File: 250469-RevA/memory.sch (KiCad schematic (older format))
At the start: 10 parts, among them U10 41464, U11 41464, U19 2114, U22 7416, U3 74LS08, U8 251715-01

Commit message: Change footprint of PLA to Socket version
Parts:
- U8: footprint krl_Package_SPDIP:SPDIP-64_W19.05mm_LongPads -> krl_Package_SPDIP:SPDIP-64_W19.05mm_Socket_LongPads
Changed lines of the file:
@@
 F 0 "U8" H 8000 5700 50  0000 C CNN
 F 1 "251715-01" H 8900 5700 50  0000 C CNN
-F 2 "krl_Package_SPDIP:SPDIP-64_W19.05mm_LongPads" H 7600 2100 50  0001 C CNN
+F 2 "krl_Package_SPDIP:SPDIP-64_W19.05mm_Socket_LongPads" H 7600 2100 50  0001 C CNN
 F 3 "" H 8600 5050 50  0001 C CNN
 	1    8550 3950

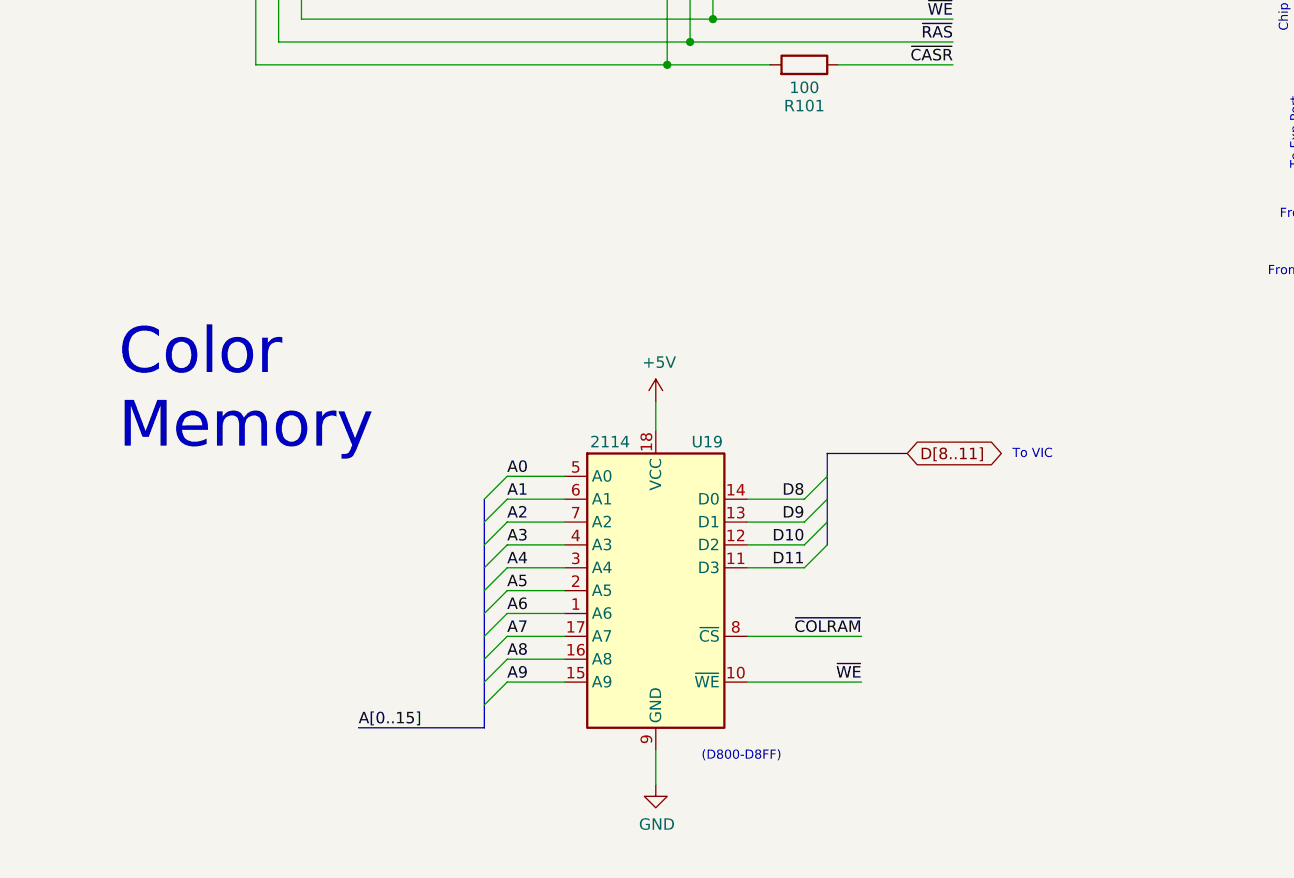
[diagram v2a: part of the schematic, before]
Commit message: Changed footprint of DIC connectors and wiring of Color RAM
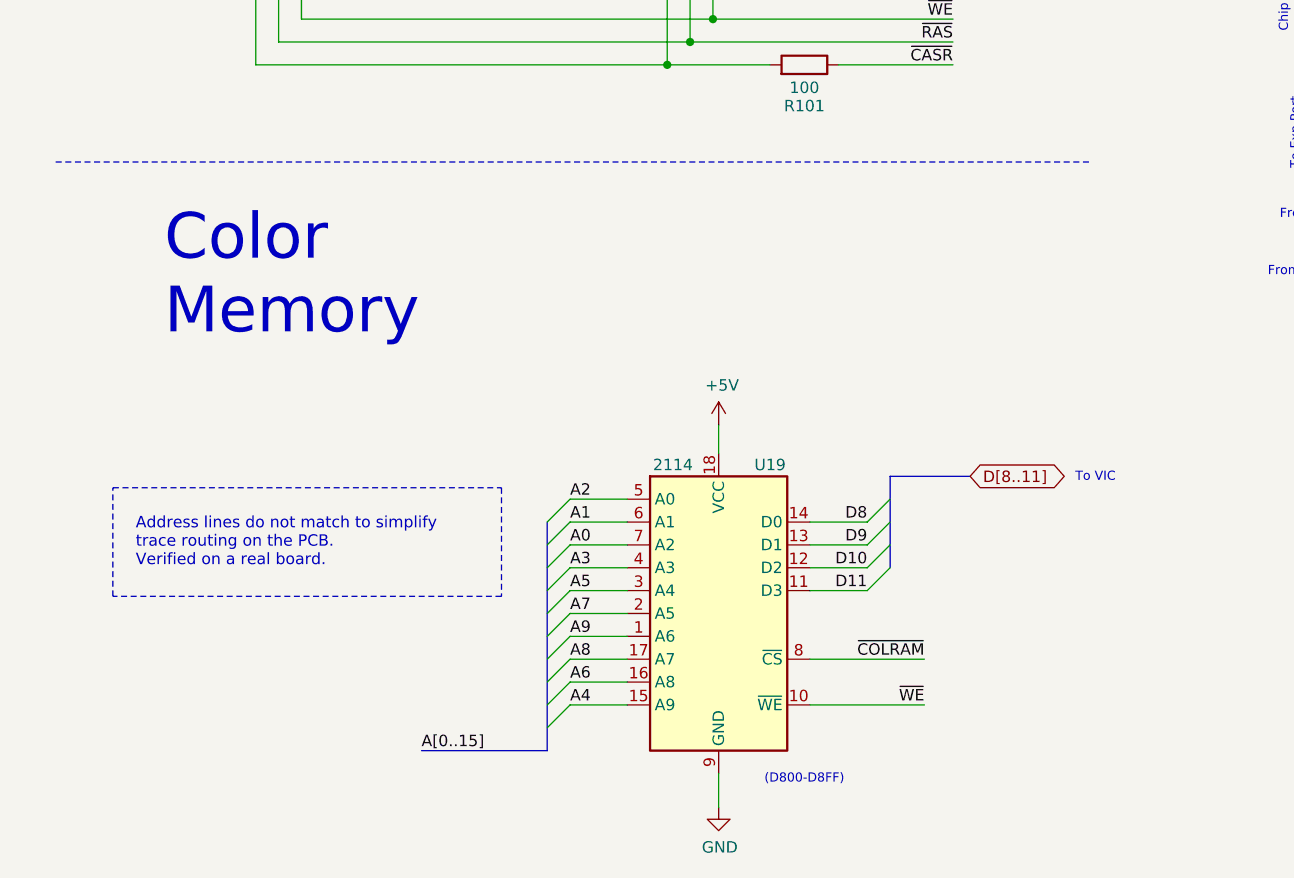
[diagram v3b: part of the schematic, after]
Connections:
- net A0: now also U19.7 (A2); no longer U19.5 (A0)
- net A2: now also U19.5 (A0); no longer U19.7 (A2)
- net A4: now also U19.15 (A9); no longer U19.3 (A4)
- net A5: now also U19.3 (A4); no longer U19.2 (A5)
- net A6: now also U19.16 (A8); no longer U19.1 (A6)
- net A7: now also U19.2 (A5); no longer U19.17 (A7)
- net A8: now also U19.17 (A7); no longer U19.16 (A8)
- net A9: now also U19.1 (A6); no longer U19.15 (A9)
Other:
- note added: "Address lines do not match to simplify\ntrace routing on the PCB.\nVerified on a real board."
- moved on the sheet: U19
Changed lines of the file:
@@
 Text Label 7400 3950 0    50   ~ 0
 ~WE
-Text Label 2200 6650 0    50   ~ 0
+Text Label 2475 6750 0    50   ~ 0
 A[0..15]
 Wire Wire Line
@@
  Memory\nController
 Wire Wire Line
-	3100 5550 2850 5550
-Entry Wire Line
-	2850 5550 2750 5650
-Entry Wire Line
-	2850 5650 2750 5750
-Entry Wire Line
-	2850 5750 2750 5850
-Entry Wire Line
-	2850 5850 2750 5950
-Entry Wire Line
-	2850 5950 2750 6050
-Entry Wire Line
-	2850 6050 2750 6150
-Entry Wire Line
-	2850 6150 2750 6250
-Entry Wire Line
-	2850 6250 2750 6350
-Entry Wire Line
-	2850 6350 2750 6450
-Entry Wire Line
-	2850 6450 2750 6550
-Wire Wire Line
-	2850 6450 3100 6450
-Wire Wire Line
-	2850 6350 3100 6350
-Wire Wire Line
-	2850 6250 3100 6250
-Wire Wire Line
-	2850 6150 3100 6150
-Wire Wire Line
-	2850 6050 3100 6050
-Wire Wire Line
-	2850 5950 3100 5950
-Wire Wire Line
-	2850 5850 3100 5850
-Wire Wire Line
-	2850 5650 3100 5650
-Wire Wire Line
-	2850 5750 3100 5750
-Text Label 2850 5550 0    50   ~ 0
+	3375 5650 3125 5650
+Entry Wire Line
+	3125 5650 3025 5750
+Entry Wire Line
+	3125 5750 3025 5850
+Entry Wire Line
+	3125 5850 3025 5950
+Entry Wire Line
+	3125 5950 3025 6050
+Entry Wire Line
+	3125 6050 3025 6150
+Entry Wire Line
+	3125 6150 3025 6250
+Entry Wire Line
+	3125 6250 3025 6350
+Entry Wire Line
+	3125 6350 3025 6450
+Entry Wire Line
+	3125 6450 3025 6550
+Entry Wire Line
+	3125 6550 3025 6650
+Wire Wire Line
+	3125 6550 3375 6550
+Wire Wire Line
+	3125 6450 3375 6450
+Wire Wire Line
+	3125 6350 3375 6350
+Wire Wire Line
+	3125 6250 3375 6250
+Wire Wire Line
+	3125 6150 3375 6150
+Wire Wire Line
+	3125 6050 3375 6050
+Wire Wire Line
+	3125 5950 3375 5950
+Wire Wire Line
+	3125 5750 3375 5750
+Wire Wire Line
+	3125 5850 3375 5850
+Text Label 3125 5850 0    50   ~ 0
 A0
-Text Label 2850 5650 0    50   ~ 0
+Text Label 3125 5750 0    50   ~ 0
 A1
-Text Label 2850 5750 0    50   ~ 0
+Text Label 3125 5650 0    50   ~ 0
 A2
-Text Label 2850 5850 0    50   ~ 0
+Text Label 3125 5950 0    50   ~ 0
 A3
-Text Label 2850 5950 0    50   ~ 0
+Text Label 3125 6550 0    50   ~ 0
 A4
-Text Label 2850 6050 0    50   ~ 0
+Text Label 3125 6050 0    50   ~ 0
 A5
-Text Label 2850 6150 0    50   ~ 0
+Text Label 3125 6450 0    50   ~ 0
 A6
-Text Label 2850 6250 0    50   ~ 0
+Text Label 3125 6150 0    50   ~ 0
 A7
-Text Label 2850 6350 0    50   ~ 0
+Text Label 3125 6350 0    50   ~ 0
 A8
-Text Label 2850 6450 0    50   ~ 0
+Text Label 3125 6250 0    50   ~ 0
 A9
 $Comp
 L power:GND #PWR0173
 U 1 1 5F0F4C6A
-P 3500 6900
-F 0 "#PWR0173" H 3500 6650 50  0001 C CNN
-F 1 "GND" H 3505 6727 50  0000 C CNN
-F 2 "" H 3500 6900 50  0001 C CNN
-F 3 "" H 3500 6900 50  0001 C CNN
-	1    3500 6900
+P 3775 7000
+F 0 "#PWR0173" H 3775 6750 50  0001 C CNN
+F 1 "GND" H 3780 6827 50  0000 C CNN
+F 2 "" H 3775 7000 50  0001 C CNN
+F 3 "" H 3775 7000 50  0001 C CNN
+	1    3775 7000
 	1    0    0    -1
 $EndComp
 Wire Wire Line
-	3900 6250 4400 6250
-Wire Wire Line
-	3900 6450 4400 6450
-Wire Wire Line
-	3900 5950 4150 5950
-Wire Wire Line
-	3900 5650 4150 5650
-Wire Wire Line
-	3900 5750 4150 5750
-Wire Wire Line
-	3900 5850 4150 5850
-Entry Wire Line
-	4150 5650 4250 5550
-Entry Wire Line
-	4150 5750 4250 5650
-Entry Wire Line
-	4150 5850 4250 5750
-Entry Wire Line
-	4150 5950 4250 5850
-Wire Bus Line
-	4250 5450 4600 5450
-Text GLabel 4600 5450 2    50   BiDi ~ 0
+	4175 6350 4675 6350
+Wire Wire Line
+	4175 6550 4675 6550
+Wire Wire Line
+	4175 6050 4425 6050
+Wire Wire Line
+	4175 5750 4425 5750
+Wire Wire Line
+	4175 5850 4425 5850
+Wire Wire Line
+	4175 5950 4425 5950
+Entry Wire Line
+	4425 5750 4525 5650
+Entry Wire Line
+	4425 5850 4525 5750
+Entry Wire Line
+	4425 5950 4525 5850
+Entry Wire Line
+	4425 6050 4525 5950
+Wire Bus Line
+	4525 5550 4875 5550
+Text GLabel 4875 5550 2    50   BiDi ~ 0
 D[8..11]
-Text Label 4150 5650 2    50   ~ 0
+Text Label 4425 5750 2    50   ~ 0
 D8
-Text Label 4150 5750 2    50   ~ 0
+Text Label 4425 5850 2    50   ~ 0
 D9
-Text Label 4150 5850 2    50   ~ 0
+Text Label 4425 5950 2    50   ~ 0
 D10
-Text Label 4150 5950 2    50   ~ 0
+Text Label 4425 6050 2    50   ~ 0
 D11
 Wire Wire Line
@@
 Text Label 7400 4050 0    50   ~ 0
 ~COLRAM
-Text Label 4400 6250 2    50   ~ 0
+Text Label 4675 6350 2    50   ~ 0
 ~COLRAM
 Text Notes 3000 950  0    200  ~ 0
 RAM
-Text Notes 1150 5450 0    200  ~ 0
+Text Notes 1350 4950 0    200  ~ 0
 Color\nMemory
-Text Label 4400 6450 2    50   ~ 0
+Text Label 4675 6550 2    50   ~ 0
 ~WE
-Text Notes 3700 6800 0    40   ~ 0
+Text Notes 3975 6900 0    40   ~ 0
 (D800-D8FF)
 Text GLabel 7050 5500 0    50   BiDi ~ 0
@@
 	7700 5550 7950 5550
 Wire Bus Line
-	2750 6650 2200 6650
+	3025 6750 2475 6750
 Text GLabel 10300 2150 2    50   Output ~ 0
 ~KBR_CS
@@
 Text Notes 6480 4680 2    40   ~ 0
 From CIA 2
-Text Notes 5060 5480 0    40   ~ 0
+Text Notes 5335 5580 0    40   ~ 0
 To VIC
 Wire Wire Line
@@
 L power:+5V #PWR0172
 U 1 1 5EFDEDE2
-P 3500 5225
-F 0 "#PWR0172" H 3500 5075 50  0001 C CNN
-F 1 "+5V" H 3515 5398 50  0000 C CNN
-F 2 "" H 3500 5225 50  0001 C CNN
-F 3 "" H 3500 5225 50  0001 C CNN
-	1    3500 5225
+P 3775 5325
+F 0 "#PWR0172" H 3775 5175 50  0001 C CNN
+F 1 "+5V" H 3790 5498 50  0000 C CNN
+F 2 "" H 3775 5325 50  0001 C CNN
+F 3 "" H 3775 5325 50  0001 C CNN
+	1    3775 5325
 	1    0    0    -1
 $EndComp
@@
 L krl_Memory_RAM:2114 U19
 U 1 1 5E3F3F3A
-P 3500 6050
-F 0 "U19" H 3725 6700 50  0000 C CNN
-F 1 "2114" H 3300 6700 50  0000 C CNN
-F 2 "Package_DIP:DIP-18_W7.62mm_Socket" H 2750 5400 50  0001 C CIN
-F 3 "" H 3500 6150 50  0001 C CNN
-	1    3500 6050
+P 3775 6150
+F 0 "U19" H 4000 6800 50  0000 C CNN
+F 1 "2114" H 3575 6800 50  0000 C CNN
+F 2 "Package_DIP:DIP-18_W7.62mm_Socket" H 3025 5500 50  0001 C CIN
+F 3 "" H 3775 6250 50  0001 C CNN
+	1    3775 6150
 	1    0    0    -1
 $EndComp
 Wire Wire Line
-	3500 5225 3500 5350
-Wire Wire Line
-	3500 6900 3500 6750
+	3775 5325 3775 5450
+Wire Wire Line
+	3775 7000 3775 6850
 Wire Wire Line
 	2500 3200 2500 2925
@@
 Wire Wire Line
 	4300 2925 4300 3000
+Wire Notes Line
+	875  4175 5400 4175
+Text Notes 1225 5950 0    50   ~ 0
+Address lines do not match to simplify\ntrace routing on the PCB.\nVerified on a real board.
+Wire Notes Line width 10 style solid
+	1125 5600 2825 5600
+Wire Notes Line width 10 style solid
+	2825 5600 2825 6075
+Wire Notes Line width 10 style solid
+	2825 6075 1125 6075
+Wire Notes Line width 10 style solid
+	1125 6075 1125 5600
 Wire Bus Line
 	7250 4450 7250 4650
@@
 	7150 4250 7150 4400
 Wire Bus Line
-	4250 5450 4250 5850
+	4525 5550 4525 5950
 Wire Bus Line
 	1650 1950 1650 3050
@@
 	7500 4750 7500 5500
 Wire Bus Line
-	2750 5650 2750 6650
+	3025 5750 3025 6750
 Wire Bus Line
 	5050 1500 5050 2450

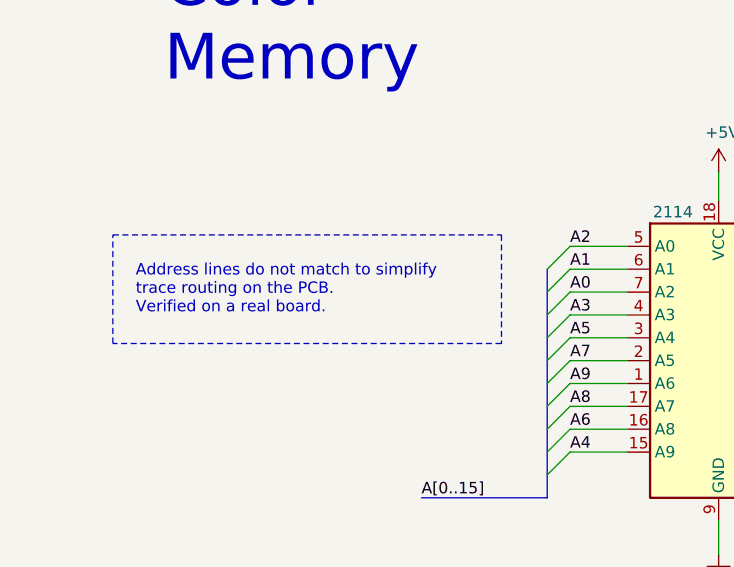
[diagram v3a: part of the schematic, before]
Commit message: Minor changes to the memory sheet
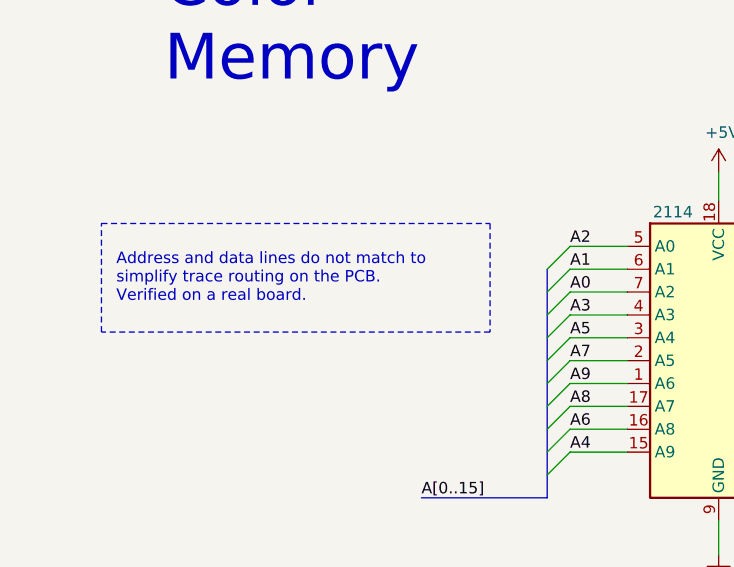
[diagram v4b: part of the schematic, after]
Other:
- note added: "Address and data lines do not match to\nsimplify trace routing on the PCB.\nVerified on a real board."
- note removed: "Address lines do not match to simplify\ntrace routing on the PCB.\nVerified on a real board."
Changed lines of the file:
@@
 Wire Notes Line
 	875  4175 5400 4175
-Text Notes 1225 5950 0    50   ~ 0
-Address lines do not match to simplify\ntrace routing on the PCB.\nVerified on a real board.
+Text Notes 1140 5900 0    50   ~ 0
+Address and data lines do not match to\nsimplify trace routing on the PCB.\nVerified on a real board.
 Wire Notes Line width 10 style solid
-	1125 5600 2825 5600
+	1075 5550 2775 5550
 Wire Notes Line width 10 style solid
-	2825 5600 2825 6075
+	2775 5550 2775 6025
 Wire Notes Line width 10 style solid
-	2825 6075 1125 6075
+	2775 6025 1075 6025
 Wire Notes Line width 10 style solid
-	1125 6075 1125 5600
+	1075 6025 1075 5550
 Wire Bus Line
 	7250 4450 7250 4650
